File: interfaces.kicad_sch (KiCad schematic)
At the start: 33 parts, among them J13 SM04B-SRSS-TB-LF-SN, J14 SM04B-SRSS-TB-LF-SN, J3 SI-51005-F, U7 MAX3051EKA

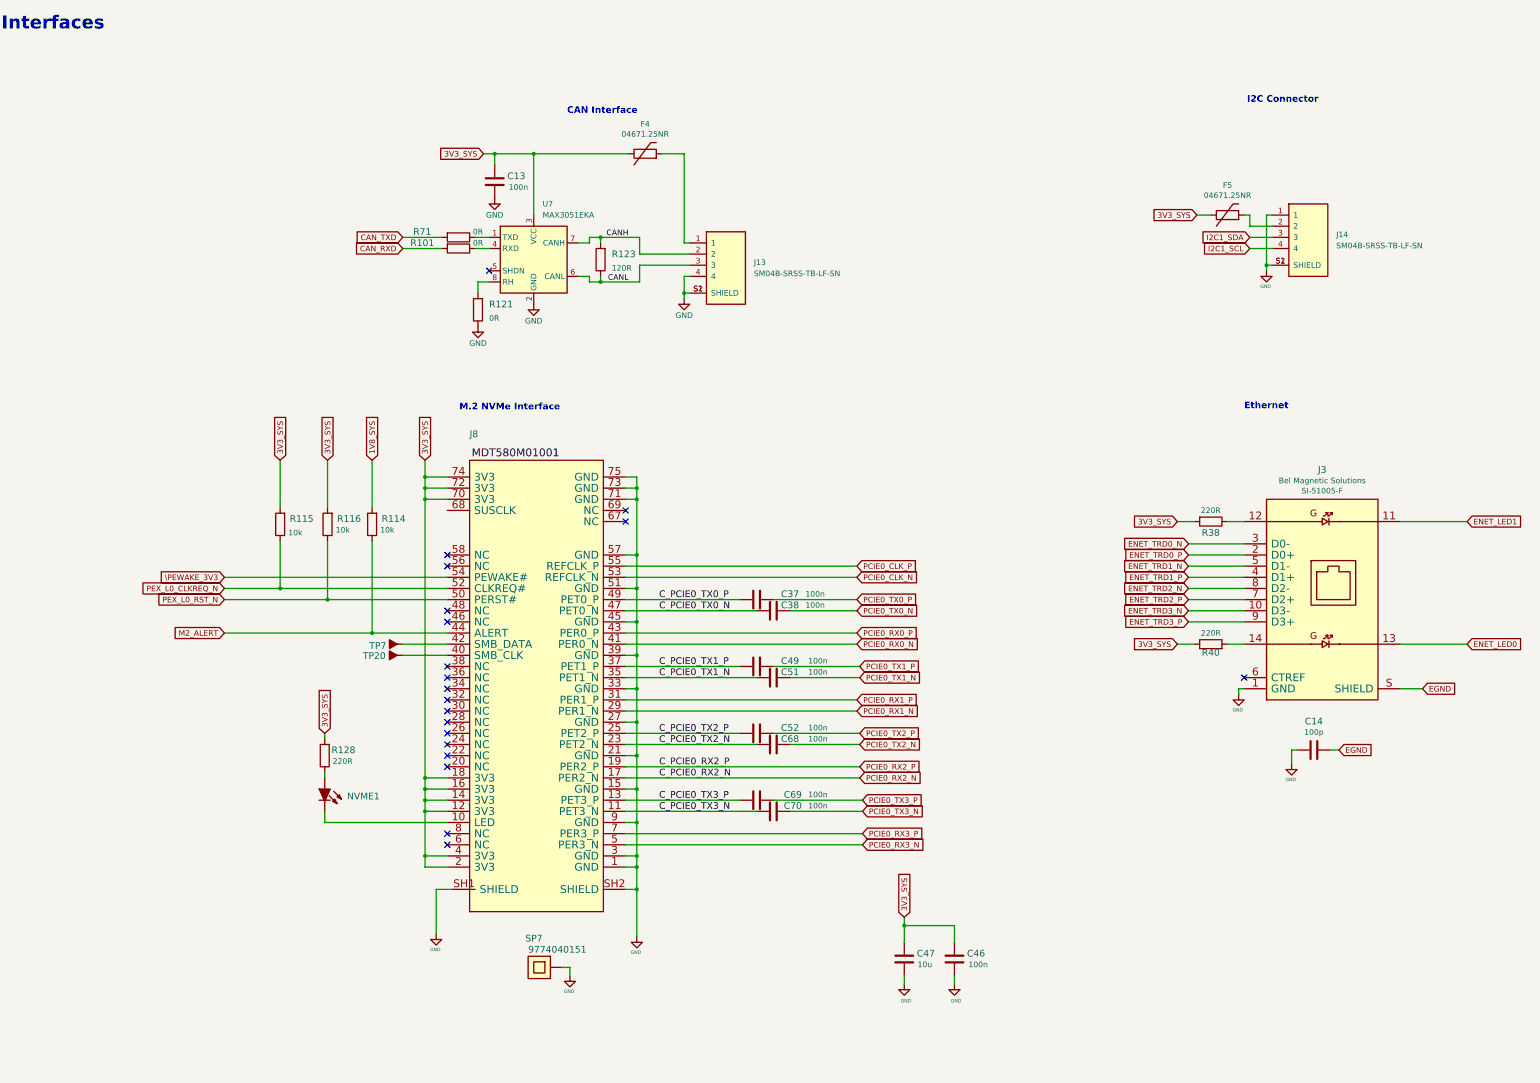
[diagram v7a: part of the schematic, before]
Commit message: Standardize components
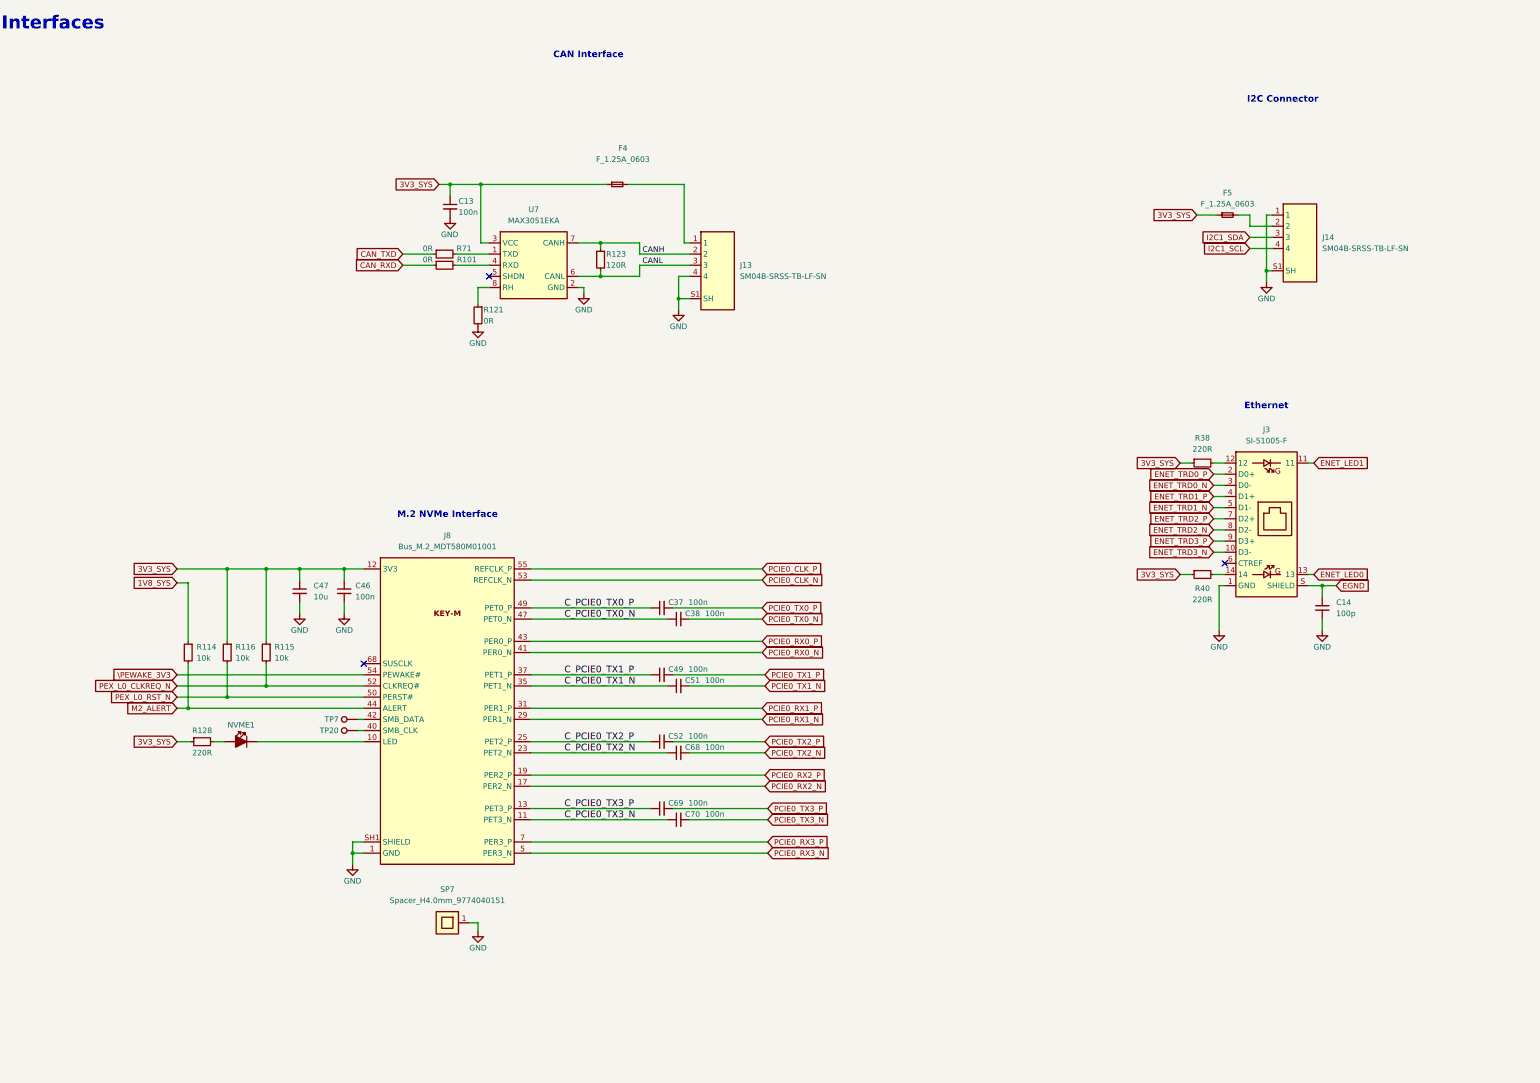
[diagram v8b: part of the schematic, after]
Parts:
- removed SP7: 9774040151, jetson-nano-baseboard-footprints:9774060151, symbol jetson-nano-baseboard:9774040151
- added SP7: Spacer_H4.0mm_9774040151, antmicro-footprints:Spacer_SMD_M2.5_H4mm_Wurth_9774040151, symbol antmicroMechanicalParts:Spacer_H4.0mm_9774040151
- C13, C37, C38, C46, C49, C51, C52, C68, C69, C70: footprint jetson-nano-baseboard-footprints:0402-cap -> antmicro-footprints:C_0402_1005Metric; symbol jetson-nano-baseboard:C_100n_0402 -> antmicroCapacitors0402:C_100n_0402; Author (none) -> Antmicro; Dielectric (none) -> X5R; License (none) -> Apache-2.0; MPN 0402X104K6R3CT -> GRM155R61H104KE14D; Manufacturer Walsin -> Murata; Voltage (none) -> 50V
- C14: footprint jetson-nano-baseboard-footprints:0402-cap -> antmicro-footprints:C_0402_1005Metric; symbol jetson-nano-baseboard:C_100p_0402 -> antmicroCapacitors0402:C_100p_0402; Author (none) -> Antmicro; Dielectric (none) -> C0G; License (none) -> Apache-2.0; MPN 0402N101J500CT -> GCM1555C1H101JA16D; Manufacturer WALSIN -> Murata; Voltage (none) -> 50V
- C47: footprint jetson-nano-baseboard-footprints:0603-cap -> antmicro-footprints:C_0603_1608Metric; symbol jetson-nano-baseboard:C_10u_0603 -> antmicroCapacitors0603:C_10u_0603; Author (none) -> Antmicro; License (none) -> Apache-2.0
- F4, F5: value 04671.25NR -> F_1.25A_0603; footprint jetson-nano-baseboard-footprints:0603-Fuse-Littelfuse-0467 -> antmicro-footprints:F_0603_1608Metric; symbol jetson-nano-baseboard:04671.25NR -> antmicroFuses:F_1.25A_0603; Author (none) -> Antmicro; License (none) -> Apache-2.0; Manufacturer Littelfuse Inc. -> Littelfuse
- J13, J14: footprint jetson-nano-baseboard-footprints:SM04B-SRSS-TB-LF-SN -> antmicro-footprints:SM04B-SRSS-TB-LF-SN; symbol jetson-nano-baseboard:SM04B-SRSS-TB-LF-SN -> antmicroRectangularConnectorsHeadersMalePins:SM04B-SRSS-TB-LF-SN; Author (none) -> Antmicro; License (none) -> Apache-2.0; MPN SM04B-SRSS-TB-LF-SN -> SM04B-SRSS-TB(LF)(SN)
- J3: footprint jetson-nano-baseboard-footprints:SI-51005-F -> antmicro-footprints:RJ45_Bel_SI-51005-F; symbol jetson-nano-baseboard:SI-51005-F -> antmicroModularConnectorsJacksWithMagnetics:RJ45_Bel_SI-51005-F; Author (none) -> Antmicro; License (none) -> Apache-2.0
- J8: value ~ -> Bus_M.2_MDT580M01001; footprint jetson-nano-baseboard-footprints:MDT580M01001 -> antmicro-footprints:Bus_M.2_Socket_Key_M_Amphenol_MDT580M01001; symbol jetson-nano-baseboard:MDT580M01001 -> antmicroPciConnectors:Bus_M.2_MDT580M01001; Author (none) -> Antmicro; License (none) -> Apache-2.0
- NVME1: footprint jetson-nano-baseboard-footprints:LED0603 -> antmicro-footprints:LED_0603_1608Metric_G; symbol jetson-nano-baseboard:LED -> antmicroLEDIndicationDiscrete:LED_G_0603_LG_L29K-G2J1-24-Z; Author (none) -> Antmicro; License (none) -> Apache-2.0; MPN KPT-1608SGC -> LG L29K-G2J1-24-Z; Manufacturer Kingbright -> Osram
- R101, R121, R71: footprint jetson-nano-baseboard-footprints:0402-res -> antmicro-footprints:R_0402_1005Metric; symbol jetson-nano-baseboard:R_0R_0402 -> antmicroResistors0402:R_0R_0402; Author (none) -> Antmicro; Current (none) -> 1A; License (none) -> Apache-2.0; Manufacturer PANASONIC -> Panasonic
- R114, R115, R116: footprint jetson-nano-baseboard-footprints:0402-res -> antmicro-footprints:R_0402_1005Metric; symbol jetson-nano-baseboard:R_10k_0402 -> antmicroResistors0402:R_10k_0402; Author (none) -> Antmicro; License (none) -> Apache-2.0; MPN CRCW040210K0FKEDHP -> CR0402-FX-1002GLF; Manufacturer VISHAY -> Bourns; Tolerance (none) -> 1%
- R123: footprint jetson-nano-baseboard-footprints:0402-res -> antmicro-footprints:R_0402_1005Metric; symbol jetson-nano-baseboard:R_120R_0402 -> antmicroResistors0402:R_120R_0402; Author (none) -> Antmicro; License (none) -> Apache-2.0; MPN ERJ2GEJ121X -> CR0402-FX-1200GLF; Manufacturer PANASONIC -> Bourns; Tolerance (none) -> 1%
- R128, R38, R40: footprint jetson-nano-baseboard-footprints:0402-res -> antmicro-footprints:R_0402_1005Metric; symbol jetson-nano-baseboard:R_220R_0402 -> antmicroResistors0402:R_220R_0402; Author (none) -> Antmicro; License (none) -> Apache-2.0; MPN ERJ2GEJ221X -> CR0402-FX-2200GLF; Manufacturer Panasonic -> Bourns; Tolerance (none) -> 1%
- TP20, TP7: value ~ -> TP_1.5mm_SMD; footprint jetson-nano-baseboard-footprints:TP-R-1.5 -> antmicro-footprints:TP_SMD_1.5mm; symbol jetson-nano-baseboard:Testpad -> antmicroTestPoints:TP_1.5mm_SMD; Author (none) -> Antmicro; License (none) -> Apache-2.0
- U7: footprint jetson-nano-baseboard-footprints:SOT-23-8 -> antmicro-footprints:SOT-23-8; symbol jetson-nano-baseboard:MAX3051EKA -> antmicroInterfaceDriversReceiversTransceivers:MAX3051EKA; Author (none) -> Antmicro; License (none) -> Apache-2.0
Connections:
- net 1V8_SYS: now also R114.1; no longer R114.2
- net 3V3_SYS: now also C13.1, C46.1, C47.1, R115.1, R116.1, R128.1, R38.1; no longer C13.2, C46.2, C47.2, R115.2, R116.2, R128.2, R38.2
- net CANH: now also R123.1; no longer R123.2
- net CANL: now also R123.2; no longer R123.1
- net CAN_RXD: now also R101.1; no longer R101.2
- net CAN_TXD: now also R71.1; no longer R71.2
- net GND: now also C13.2, C46.2, C47.2, R121.2, SP7.1; no longer C13.1, C46.1, C47.1, R121.1
- net M2_ALERT: now also R114.2; no longer R114.1
- net PEX_L0_CLKREQ_N: now also R115.2; no longer R115.1
- net PEX_L0_RST_N: now also R116.2; no longer R116.1
- net at NVME1.1: now also R128.2; no longer R128.1
- net at J8.20 (NC): now also J8.22 (NC), J8.24 (NC), J8.26 (NC), J8.28 (NC), J8.30 (NC), J8.32 (NC), J8.34 (NC), J8.36 (NC), J8.38 (NC), J8.46 (NC), J8.48 (NC), J8.56 (NC), J8.58 (NC), J8.6 (NC), J8.67 (NC), J8.69 (NC), J8.8 (NC)
- net at J3.12: now also R38.2; no longer R38.1
- net at U7.1 (TXD): now also R71.2; no longer R71.1
- net at U7.8 (RH): now also R121.1; no longer R121.2
- net at U7.4 (RXD): now also R101.2; no longer R101.1
- no-connect marks 20 -> 3
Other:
- moved on the sheet: C13, C14, C37, C38, C46, C47, C49, C51, C52, C68, C69, C70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
